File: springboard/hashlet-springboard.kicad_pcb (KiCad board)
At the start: 2 copper layers, 16.5 x 15 mm, 3 parts, among them K1 CONN_3, P1 CONN_7X2, U1 ATSHA204A

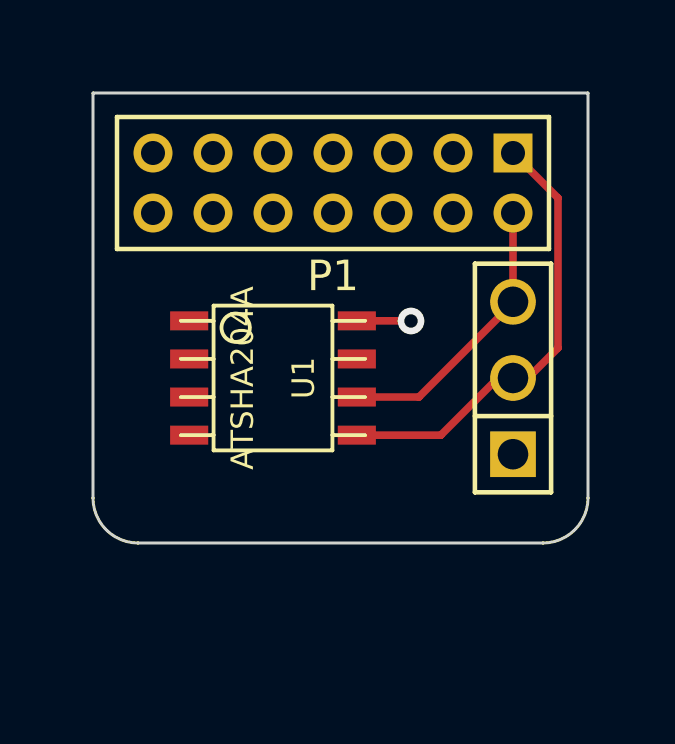
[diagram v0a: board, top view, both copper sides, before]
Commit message: springboard: PCB preparation v1
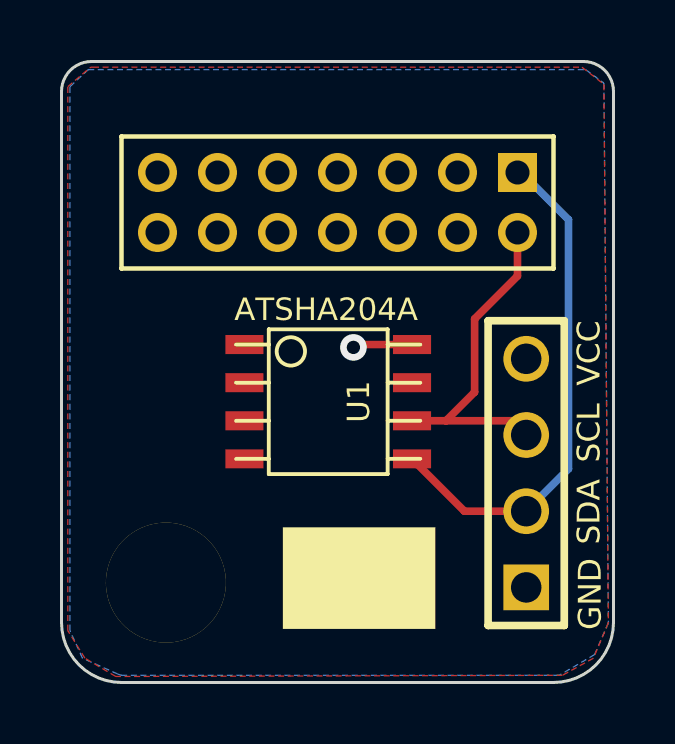
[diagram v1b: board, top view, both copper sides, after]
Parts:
- removed K1: CONN_3, PIN_ARRAY_3X1
- added G***: LOGO, LOGO, F.Cu at (203.9, 152.2)
- added G***: LOGO, OSHW, B.Cu at (203.5, 150.9)
- added P2: CONN_4, PIN_ARRAY_4x1, F.Cu at (209.4, 148.7)
- added PIN_ARRAY_1: Val**, PIN_ARRAY_1, F.Cu at (197.4, 152.3)
- moved U1 2.00 mm to (202.8, 146.3)
- moved P1 0.67 mm to (203.2, 139.7)
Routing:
- net /I2C0SDA: track 15.0 -> 17.2 mm
- net /I2C0SCL: track 9.50 -> 11.3 mm
- added copper zone on B.Cu, net /VCC33
- added copper zone on F.Cu, net GND
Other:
- board size 16.5 x 15 mm -> 18.4 x 20.7 mm
- board text added: "CC-BY-SA 3.0"
- board text added: "GND"
- board text added: "Hashlet for Springboard v1"
- board text added: "SCL"
- board text added: "SDA"
- board text added: "VCC"

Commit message: springboard: adjusted wiring before submission to manufacturing
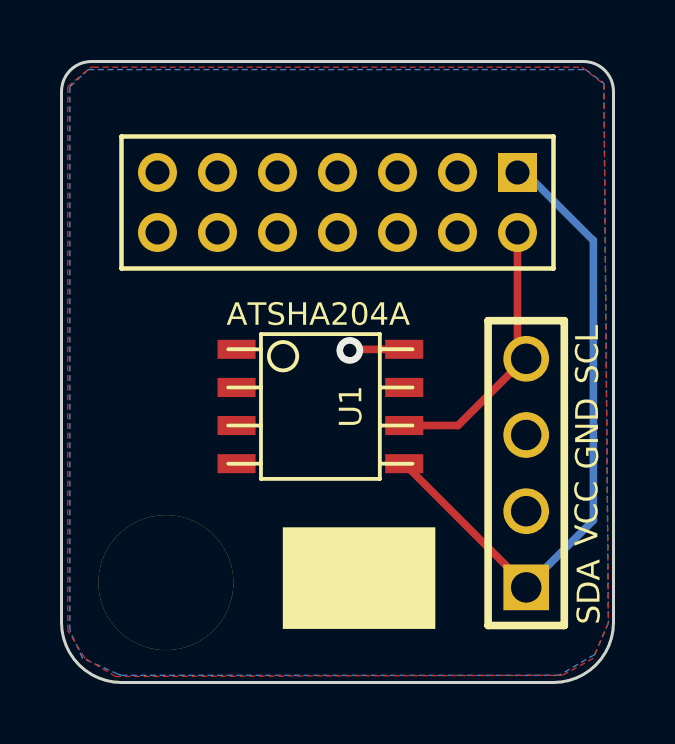
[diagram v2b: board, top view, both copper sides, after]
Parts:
- moved G*** 0.51 mm to (203.8, 151.4)
- moved U1 0.31 mm to (202.6, 146.4)
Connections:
- P2 pad 1: GND -> /I2C0SDA
- P2 pad 2: /I2C0SDA -> /VCC33
- P2 pad 3: /I2C0SCL -> GND
- P2 pad 4: /VCC33 -> /I2C0SCL
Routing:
- net /I2C0SDA: track 17.2 -> 21.8 mm
- net /I2C0SCL: track 11.3 -> 9.32 mm
